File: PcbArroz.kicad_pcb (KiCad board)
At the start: 4 copper layers, 57 parts, among them J1 Conn_Coaxial_Small, J2 USB_C_Receptacle_USB2.0_16P, Q2 SS8050, Q3 AO3400A, Q4 SS8050, SW1 SW_Push, U1 ESP32-PICO-D4, U2 RFM95W-915S2, U3 TPS62A01ADRL, U4 BQ24074RGT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

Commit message: Mejoras de lo ya ruteado / falta uc
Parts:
- moved R1 116.0 mm to (172.2, 97.5), turned to 90 degrees
- moved Q2 49.2 mm to (57.5, 53.5)
- moved R13 30.5 mm to (45.8, 53.5), turned to 90 degrees
- moved R14 26.5 mm to (53.0, 61.5), turned to 180 degrees
- moved R15 24.1 mm to (54.0, 60.5)
- moved R21 21.6 mm to (57.5, 55.8)
- moved R22 21.3 mm to (57.5, 56.8), turned to 180 degrees
- moved R16 21.2 mm to (55.0, 57.8), turned to 90 degrees
- moved R4 17.5 mm to (39.5, 70.2), turned to 180 degrees
- moved C7 16.1 mm to (42.0, 68.5), turned to 90 degrees
- moved R5 16.1 mm to (39.5, 69.2), turned to 0 degrees
- moved L1 15.4 mm to (39.0, 68.0)
- moved R17 15.3 mm to (59.8, 54.8)
- moved R3 14.8 mm to (57.5, 57.8)
- moved R6 13.6 mm to (38.5, 63.8), turned to 0 degrees
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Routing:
- net Net-(U6-TXD): track 0.00 -> 15.3 mm
- net Net-(Q2-E): track 0.00 -> 15.0 mm, vias 0 -> 2
- net Net-(U6-RXD): track 0.00 -> 13.2 mm
- net Net-(Q2-B): track 0.00 -> 11.5 mm
- net 5V: track 23.8 -> 35.1 mm, vias 0 -> 2
- net +3.3V: track 9.14 -> 18.4 mm, vias 0 -> 2
- net VBUS: track 17.3 -> 25.8 mm, vias 2 -> 4
- net Net-(D2-K): track 15.8 -> 9.97 mm
- net Net-(Q4-E): track 0.00 -> 5.29 mm
- net USB_D-: track 14.7 -> 19.5 mm, vias 2 -> 3
- net Net-(U6-VBUS): track 0.00 -> 4.42 mm
- net GND: track 23.7 -> 20.2 mm, vias 20 -> 21
- net USB_D+: track 15.4 -> 18.8 mm
- net Net-(U3-FB): track 3.01 -> 6.40 mm
- net Net-(U6-~{RST}): track 0.00 -> 2.72 mm
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
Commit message: falta uc
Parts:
- AJ-SR04M1: moved to B.Cu
- moved R1 117.9 mm to (56.8, 74.0), turned to 0 degrees
- moved AJ-SR04M1 71.3 mm to (44.2, 75.0), turned to -90 degrees
- moved SW1 63.3 mm to (75.2, 73.2)
- moved C6 62.2 mm to (66.5, 61.2), turned to 0 degrees
- moved C15 61.3 mm to (57.0, 61.7), turned to 90 degrees
- moved C2 61.2 mm to (58.3, 61.7), turned to 90 degrees
- moved Q3 56.0 mm to (54.5, 71.5), turned to 180 degrees
- moved C14 55.7 mm to (56.9, 65.7), turned to -90 degrees
- moved C11 55.7 mm to (58.2, 65.6), turned to -90 degrees
- moved U1 54.5 mm to (62.8, 66.3), turned to 0 degrees
- moved Q4 50.6 mm to (62.8, 57.2)
- moved R18 46.4 mm to (65.2, 71.8), turned to -90 degrees
- moved C3 46.2 mm to (63.1, 72.2), turned to -90 degrees
- moved R20 46.2 mm to (62.1, 72.2), turned to -90 degrees
- moved R2 44.1 mm to (62.6, 73.7), turned to 180 degrees
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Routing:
- net MOSI_LoRa: track 38.6 -> 1.70 mm
- net RX/TXdone_LoRa: track 33.9 -> 1.44 mm
- net MISO_LoRa: track 25.8 -> 0.00 mm
- net Net-(Q4-E): track 5.29 -> 28.4 mm, vias 0 -> 2
- net TRIG_Sensor: track 0.00 -> 22.6 mm
- net uC_EN: track 0.00 -> 19.1 mm, vias 0 -> 2
- net SCK_LoRa: track 17.1 -> 1.04 mm
- net NSS_LoRa: track 14.5 -> 0.00 mm
- net ECHO_Sensor: track 4.48 -> 16.3 mm
- net Reset_LoRa: track 11.9 -> 1.15 mm
- net Net-(J1-In): track 10.4 -> 0.00 mm
- net U0RX_uC: track 0.00 -> 10.2 mm
- net U0TX_uC: track 0.00 -> 8.46 mm
- net PWR_Sensor: track 0.00 -> 8.42 mm
- net Net-(AJ-SR04M1-GND): track 0.00 -> 8.26 mm
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
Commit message: falta uc
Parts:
- C10, C12, C13, C4, SW1: moved to B.Cu
- moved C4 97.0 mm to (26.5, 71.8), turned to -90 degrees
- moved C13 75.4 mm to (54.5, 56.3)
- moved C12 74.6 mm to (54.5, 57.2)
- moved C10 73.3 mm to (54.5, 58.3)
- moved U2 55.0 mm to (82.2, 61.8), turned to 0 degrees
- moved J1 53.0 mm to (101.5, 68.8), turned to -90 degrees
- moved SW1 52.3 mm to (23.0, 71.8), turned to 180 degrees
- moved C1 38.9 mm to (92.8, 61.8), turned to -90 degrees
- moved R20 9.55 mm to (71.2, 69.5), turned to 90 degrees
- moved R2 8.69 mm to (54.0, 75.0), turned to 90 degrees
- moved R19 7.79 mm to (70.0, 69.5), turned to 90 degrees
- moved C3 7.47 mm to (69.2, 68.0), turned to 0 degrees
- moved R18 4.15 mm to (68.8, 69.5), turned to 90 degrees
- moved BT2 1.74 mm to (30.2, 71.5)
- moved AJ-SR04M1 0.51 mm to (43.8, 74.8)
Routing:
- net CADdetect_LoRa: track 0.00 -> 56.4 mm, vias 0 -> 4
- net RXtimeout_LoRa: track 0.00 -> 51.9 mm, vias 0 -> 4
- net uC_EN: track 19.1 -> 60.6 mm, vias 2 -> 3
- net RX/TXdone_LoRa: track 1.44 -> 40.9 mm
- net MOSI_LoRa: track 1.70 -> 33.2 mm
- net SCK_LoRa: track 1.04 -> 17.7 mm
- net MISO_LoRa: track 0.00 -> 13.8 mm
- net +3.3V: track 26.5 -> 36.9 mm
- net Net-(J1-In): track 0.00 -> 10.2 mm
- net Net-(U1-IO12): track 2.08 -> 12.3 mm
- net NSS_LoRa: track 0.00 -> 8.99 mm
- net Reset_LoRa: track 1.15 -> 10.1 mm, vias 0 -> 2
- net GND: track 20.2 -> 26.2 mm, vias 31 -> 60
- net ECHO_Sensor: track 16.3 -> 21.9 mm, vias 0 -> 2
- net 3V3: track 1.52 -> 5.05 mm, vias 5 -> 6
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
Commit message: Revision general pcb
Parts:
- C10, C12, C13, C4, SW1: moved to F.Cu
- C8, R11: moved to B.Cu
- moved C4 198.6 mm to (216.0, 131.3), turned to 90 degrees
- moved SW1 198.3 mm to (212.3, 130.7)
- moved R6 197.6 mm to (215.7, 151.3), turned to 180 degrees
- moved U3 195.7 mm to (215.7, 149.0), turned to -90 degrees
- moved C7 195.5 mm to (219.8, 149.7), turned to -90 degrees
- moved R4 195.3 mm to (218.2, 149.1), turned to -90 degrees
- moved R5 195.3 mm to (217.2, 150.2), turned to -90 degrees
- moved R23 194.7 mm to (222.6, 146.8)
- moved D3 194.7 mm to (222.5, 148.3)
- moved L1 194.0 mm to (216.2, 147.1)
- moved C5 190.6 mm to (212.9, 149.0), turned to 180 degrees
- moved R2 190.4 mm to (225.7, 157.3)
- moved AJ-SR04M1 190.4 mm to (215.5, 157.1)
- moved R19 189.5 mm to (240.9, 151.4), turned to 0 degrees
- moved BT2 189.4 mm to (200.2, 155.1)
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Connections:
- J1 pad 1: Net-(J1-In) -> GND
- J1 pad 2: GND -> Net-(J1-Ext)
- J2 pad A6: Net-(J2-D+-PadA6) -> USB_D+
- J2 pad A7: Net-(J2-D--PadA7) -> USB_D-
- J2 pad B6: Net-(J2-D+-PadA6) -> USB_D+
- J2 pad B7: Net-(J2-D--PadA7) -> USB_D-
- U2 pad 9: Net-(J1-In) -> Net-(J1-Ext)
- U7 pad 1: Net-(J2-D+-PadA6) -> USB_D+
- U7 pad 3: Net-(J2-D--PadA7) -> USB_D-
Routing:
- net GND: track 26.2 -> 64.2 mm, vias 60 -> 81
- net VBUS: track 25.8 -> 57.2 mm, vias 4 -> 3
- net uC_EN: track 60.6 -> 34.4 mm, vias 3 -> 2
- net +BATT: track 27.0 -> 6.17 mm
- net BOOT: track 5.01 -> 19.6 mm, vias 0 -> 2
- net Net-(D1-K): track 17.3 -> 2.86 mm
- net 3V3: track 5.05 -> 15.4 mm, vias 6 -> 4
- net Net-(J1-Ext): track 0.00 -> 10.2 mm
- net Net-(J1-In): track 10.2 -> 0.00 mm
- net 5V: track 35.1 -> 28.0 mm
- net Net-(Q2-B): track 11.5 -> 5.48 mm
- net Net-(D2-K): track 9.97 -> 4.63 mm
- net USB_D-: track 19.5 -> 14.3 mm, vias 3 -> 0
- net USB_D+: track 18.8 -> 14.4 mm, vias 2 -> 0
- net Net-(U3-FB): track 6.40 -> 3.12 mm
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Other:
- board outline added: 88 x 33 mm

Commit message: mounting holes
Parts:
- added REF**: MountingHole_3.2mm_M3, MountingHole:MountingHole_3.2mm_M3, F.Cu at (191.7, 156.6)
- added REF**: MountingHole_3.2mm_M3, MountingHole:MountingHole_3.2mm_M3, F.Cu at (271.7, 131.6)
- added REF**: MountingHole_3.2mm_M3, MountingHole:MountingHole_3.2mm_M3, F.Cu at (191.7, 131.6)
- added REF**: MountingHole_3.2mm_M3, MountingHole:MountingHole_3.2mm_M3, F.Cu at (271.7, 156.6)
- moved CR1 3.59 mm to (195.8, 150.0)
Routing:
- net VBUS: track 57.2 -> 50.5 mm
- net GND: track 64.2 -> 66.1 mm, vias 81 -> 83
- net RX/TXdone_LoRa: track 40.6 -> 41.3 mm

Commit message: V1 a revisar
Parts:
- moved J1 14.2 mm to (258.9, 157.0), turned to 0 degrees
- moved C1 3.96 mm to (261.7, 137.8)
- moved U2 3.96 mm to (251.3, 138.0)
- moved C10 3.85 mm to (207.4, 142.5)
- moved REF** 0.46 mm to (191.4, 131.2)
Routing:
- net GND: track 66.1 -> 22.1 mm, vias 83 -> 91
- net +3.3V: track 39.5 -> 45.9 mm, vias 10 -> 13
- net 3V3: track 15.4 -> 9.95 mm
- net MOSI_LoRa: track 33.1 -> 37.5 mm
- net NSS_LoRa: track 8.99 -> 13.3 mm
- net SCK_LoRa: track 17.7 -> 21.6 mm
- net CADdetect_LoRa: track 55.9 -> 59.2 mm
- net RXtimeout_LoRa: track 51.6 -> 54.3 mm
- net RX/TXdone_LoRa: track 41.3 -> 43.7 mm
- net MISO_LoRa: track 13.8 -> 15.4 mm
- net 5V: track 28.0 -> 29.2 mm
- net Net-(U6-VBUS): track 3.57 -> 4.37 mm
- net BOOT: track 19.6 -> 20.3 mm
- net Reset_LoRa: track 9.92 -> 10.5 mm

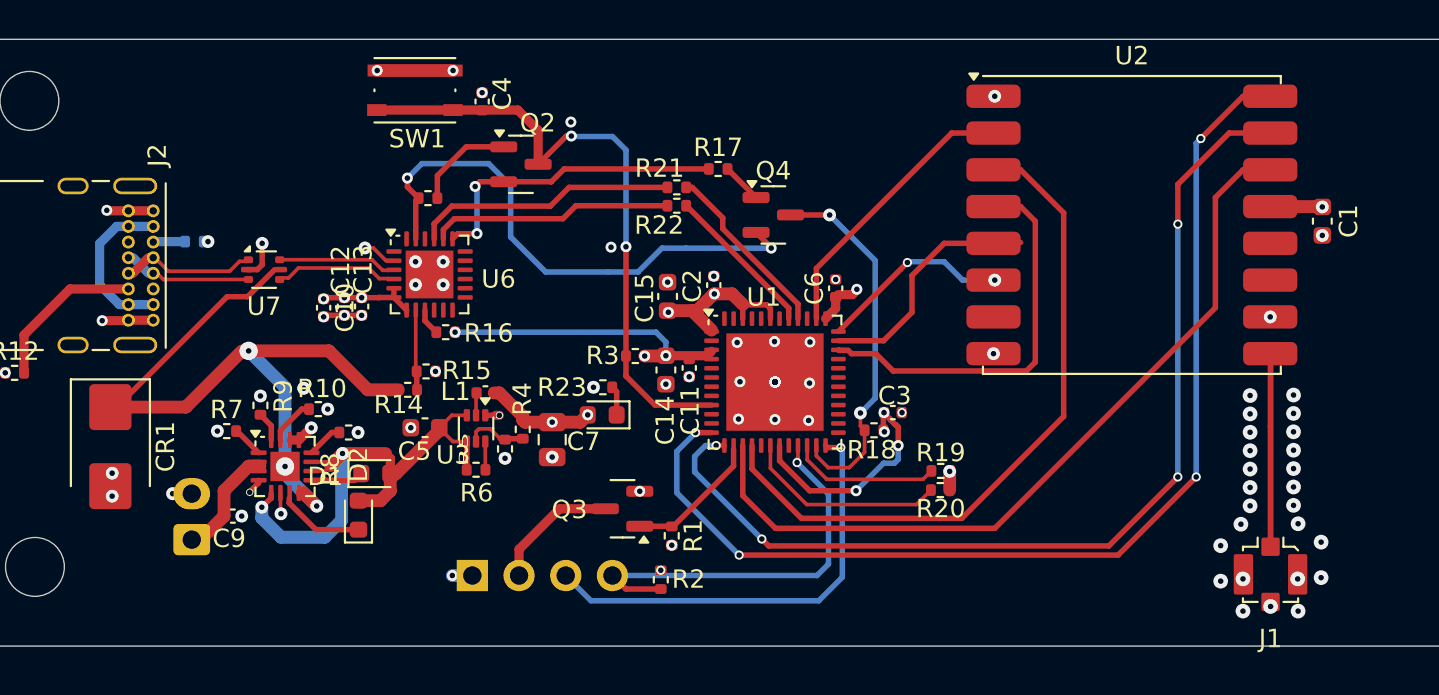
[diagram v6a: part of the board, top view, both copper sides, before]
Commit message: agregadas capas de power y gnd
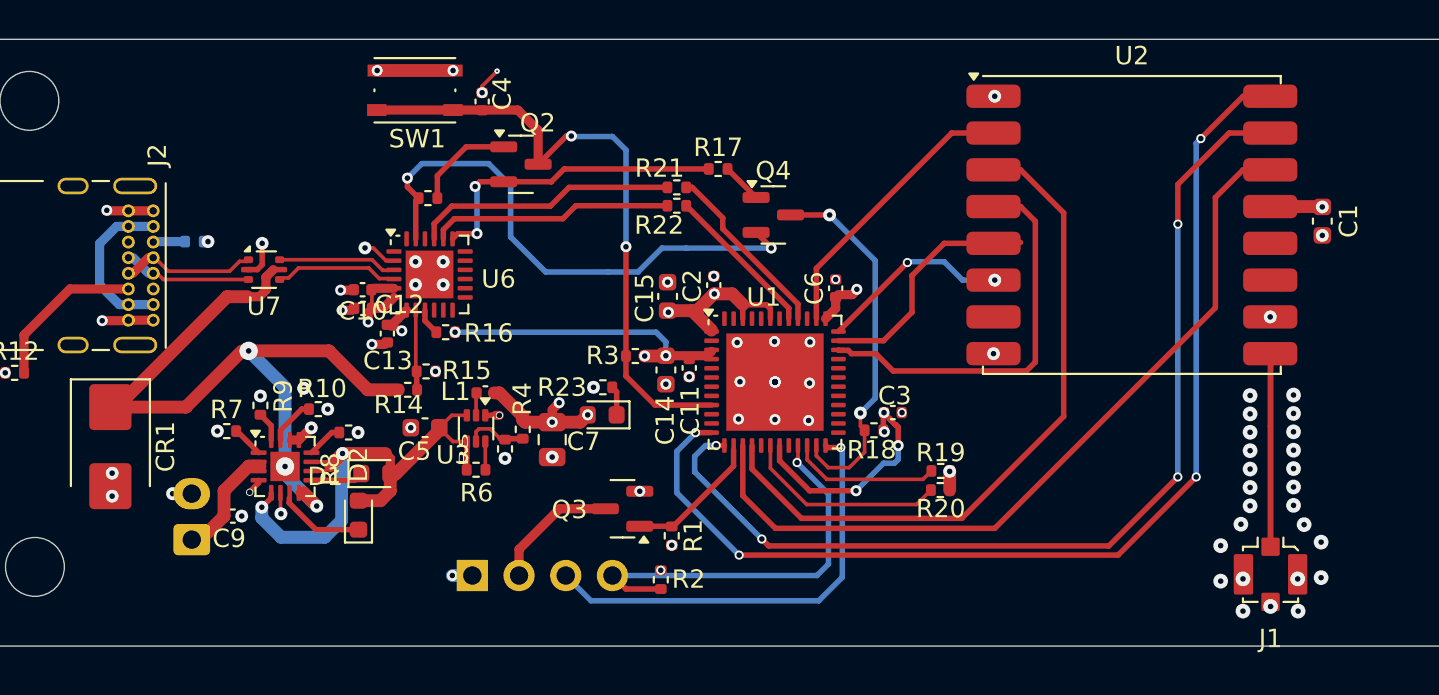
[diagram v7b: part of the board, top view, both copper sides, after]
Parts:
- moved C10 2.33 mm to (209.5, 141.5), turned to 180 degrees
- moved C13 2.03 mm to (210.8, 143.9)
- moved C12 1.02 mm to (209.5, 142.5), turned to 180 degrees
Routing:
- net GND: track 22.1 -> 23.8 mm, vias 91 -> 90
- net +3.3V: track 45.9 -> 47.4 mm, vias 13 -> 12
- net 3V3: track 9.95 -> 11.2 mm, vias 4 -> 5
- added copper zone on In2.Cu, net +3.3V
- added copper zone on In1.Cu, net GND

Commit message: Pcb v1
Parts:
- added SW2: SW_SPST, Button_Switch_THT:SW_DIP_SPSTx01_Slide_6.7x4.1mm_W7.62mm_P2.54mm_LowProfile, F.Cu at (198.1, 130.7)
- moved C9 1.60 mm to (202.4, 152.2), turned to -90 degrees
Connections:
- AJ-SR04M1 pad 1: 3V3 -> +3.3V
- BT2 pad 1: +BATT -> Net-(BT2-+)
- C1 pad 1: 3V3 -> +3.3V
- C7 pad 1: 3V3 -> +3.3V
- D3 pad 2: 3V3 -> +3.3V
- L1 pad 2: 3V3 -> +3.3V
- R4 pad 1: 3V3 -> +3.3V
- U2 pad 13: 3V3 -> +3.3V
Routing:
- net Net-(BT2-+): track 0.00 -> 31.0 mm
- net +BATT: track 6.17 -> 26.5 mm, vias 0 -> 1
- net 3V3: track 11.2 -> 0.00 mm, vias 5 -> 0
- net +3.3V: track 47.4 -> 57.9 mm, vias 12 -> 16
- net GND: vias 90 -> 88
